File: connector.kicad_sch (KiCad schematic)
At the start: 1 part, among them J4 DIN41612_02x10_AB

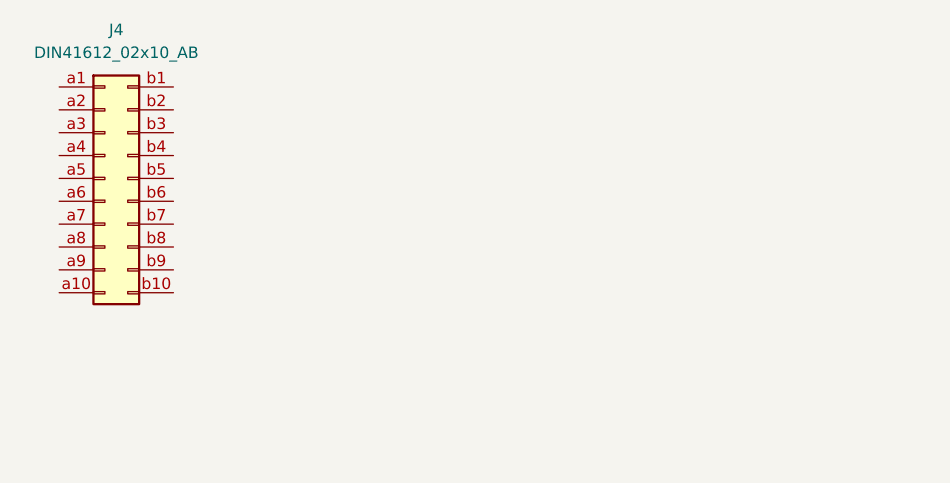
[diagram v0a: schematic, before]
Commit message: updated edge connector
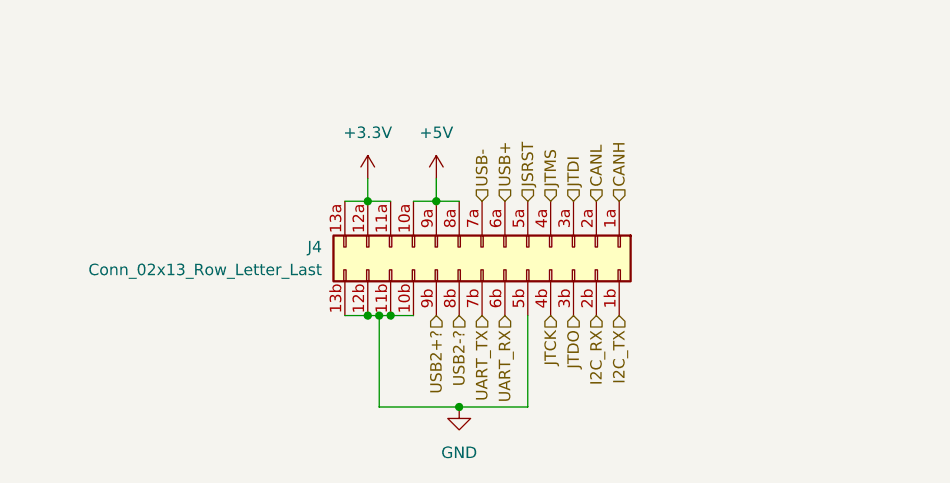
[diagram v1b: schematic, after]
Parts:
- removed J4: DIN41612_02x10_AB, symbol Connector:DIN41612_02x10_AB
- added J4: Conn_02x13_Row_Letter_Last, Connector_Samtec_HSEC8:Samtec_HSEC8-113-X-X-DV_2x13_P0.8mm_Wing_Edge, symbol Connector_Generic:Conn_02x13_Row_Letter_Last
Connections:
- new net +3.3V: J4.11a (Pin_11a), J4.12a (Pin_12a), J4.13a (Pin_13a)
- new net +5V: J4.10a (Pin_10a), J4.8a (Pin_8a), J4.9a (Pin_9a)
- new net CANH: J4.1a (Pin_1a)
- new net CANL: J4.2a (Pin_2a)
- new net GND: J4.10b (Pin_10b), J4.11b (Pin_11b), J4.12b (Pin_12b), J4.13b (Pin_13b), J4.5b (Pin_5b)
- new net I2C_RX: J4.2b (Pin_2b)
- new net I2C_TX: J4.1b (Pin_1b)
- new net JSRST: J4.5a (Pin_5a)
- new net JTCK: J4.4b (Pin_4b)
- new net JTDI: J4.3a (Pin_3a)
- new net JTDO: J4.3b (Pin_3b)
- new net JTMS: J4.4a (Pin_4a)
- new net UART_RX: J4.6b (Pin_6b)
- new net UART_TX: J4.7b (Pin_7b)
- new net USB+: J4.6a (Pin_6a)
- new net USB-: J4.7a (Pin_7a)
- new net USB2+?: J4.9b (Pin_9b)
- new net USB2-?: J4.8b (Pin_8b)

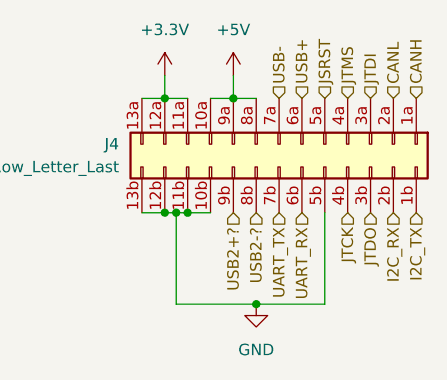
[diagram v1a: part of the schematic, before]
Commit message: renamed i2c
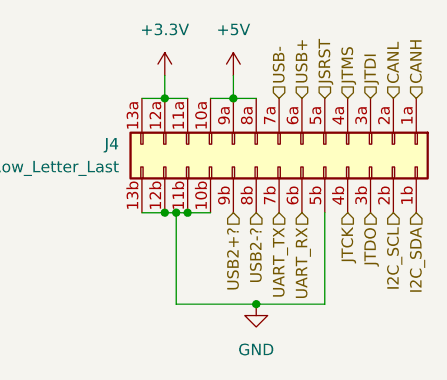
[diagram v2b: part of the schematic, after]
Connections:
- net I2C_RX renamed I2C_SCL
- net I2C_TX renamed I2C_SDA
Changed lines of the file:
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@@
 		)
 	)
-	(hierarchical_label "I2C_RX"
+	(hierarchical_label "I2C_SCL"
 		(shape input)
 		(at 86.36 53.34 270)
@@
 		)
 	)
-	(hierarchical_label "I2C_TX"
+	(hierarchical_label "I2C_SDA"
 		(shape input)
 		(at 88.9 53.34 270)

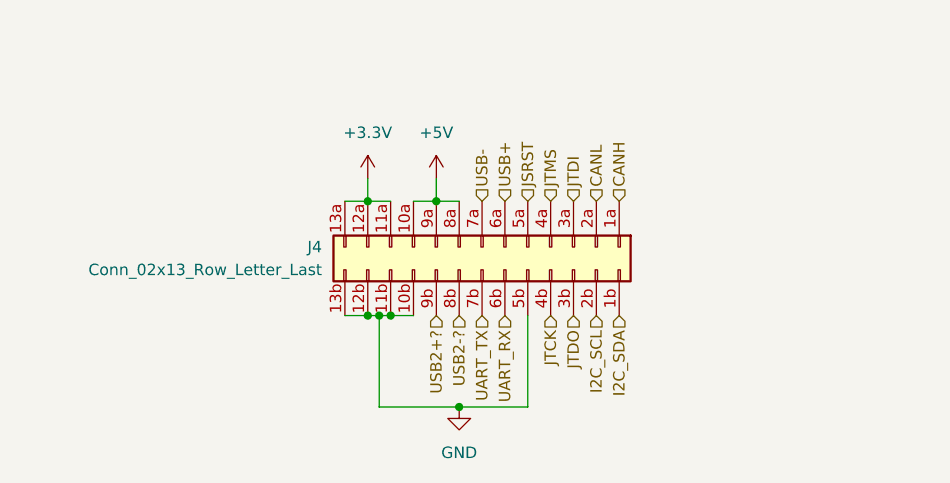
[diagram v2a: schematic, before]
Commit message: started pcb layout, host and usbhub done
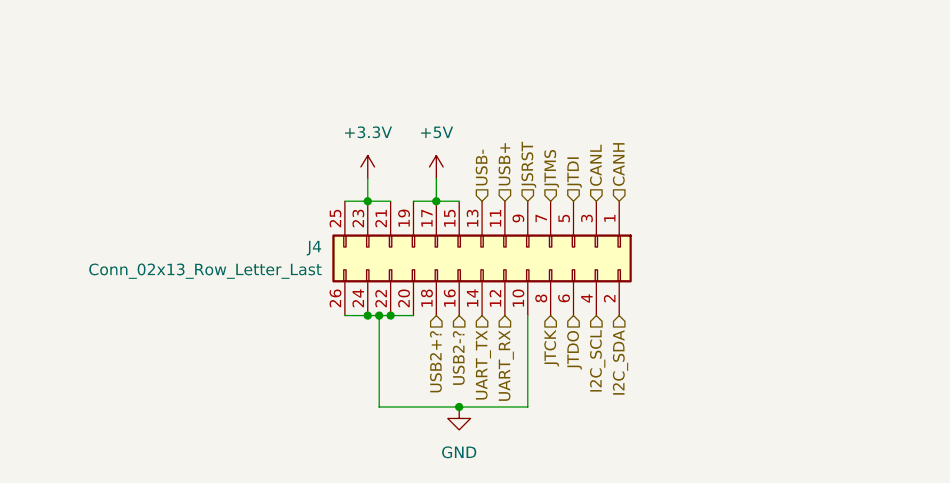
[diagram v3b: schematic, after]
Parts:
- J4: symbol Connector_Generic:Conn_02x13_Row_Letter_Last -> Connector_Generic:Conn_02x13_Odd_Even
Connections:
- net +3.3V: now also J4.21 (Pin_21), J4.23 (Pin_23), J4.25 (Pin_25); no longer J4.11a (Pin_11a), J4.12a (Pin_12a), J4.13a (Pin_13a)
- net +5V: now also J4.15 (Pin_15), J4.17 (Pin_17), J4.19 (Pin_19); no longer J4.10a (Pin_10a), J4.8a (Pin_8a), J4.9a (Pin_9a)
- net CANH: now also J4.1 (Pin_1); no longer J4.1a (Pin_1a)
- net CANL: now also J4.3 (Pin_3); no longer J4.2a (Pin_2a)
- net GND: now also J4.10 (Pin_10), J4.20 (Pin_20), J4.22 (Pin_22), J4.24 (Pin_24), J4.26 (Pin_26); no longer J4.10b (Pin_10b), J4.11b (Pin_11b), J4.12b (Pin_12b), J4.13b (Pin_13b), J4.5b (Pin_5b)
- net I2C_SCL: now also J4.4 (Pin_4); no longer J4.2b (Pin_2b)
- net I2C_SDA: now also J4.2 (Pin_2); no longer J4.1b (Pin_1b)
- net JSRST: now also J4.9 (Pin_9); no longer J4.5a (Pin_5a)
- net JTCK: now also J4.8 (Pin_8); no longer J4.4b (Pin_4b)
- net JTDI: now also J4.5 (Pin_5); no longer J4.3a (Pin_3a)
- net JTDO: now also J4.6 (Pin_6); no longer J4.3b (Pin_3b)
- net JTMS: now also J4.7 (Pin_7); no longer J4.4a (Pin_4a)
- net UART_RX: now also J4.12 (Pin_12); no longer J4.6b (Pin_6b)
- net UART_TX: now also J4.14 (Pin_14); no longer J4.7b (Pin_7b)
- net USB+: now also J4.11 (Pin_11); no longer J4.6a (Pin_6a)
- net USB-: now also J4.13 (Pin_13); no longer J4.7a (Pin_7a)
- net USB2+?: now also J4.18 (Pin_18); no longer J4.9b (Pin_9b)
- net USB2-?: now also J4.16 (Pin_16); no longer J4.8b (Pin_8b)

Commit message: pcb routed!!!!!!!
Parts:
- removed J4: Conn_02x13_Row_Letter_Last, Connector_Samtec_HSEC8:Samtec_HSEC8-113-X-X-DV_2x13_P0.8mm_Wing_Edge, symbol Connector_Generic:Conn_02x13_Odd_Even
- added J3: Conn_02x13_Row_Letter_Last, Connector_Samtec_HSEC8:Samtec_HSEC8-113-X-X-DV_2x13_P0.8mm_Edge, symbol Connector_Generic:Conn_02x13_Odd_Even
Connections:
- net +3.3V: now also J3.1 (Pin_1), J3.3 (Pin_3), J3.5 (Pin_5)
- net +5V: now also J3.11 (Pin_11), J3.7 (Pin_7), J3.9 (Pin_9)
- net CANH: now also J3.25 (Pin_25)
- net CANL: now also J3.23 (Pin_23)
- net GND: now also J3.14 (Pin_14), J3.2 (Pin_2), J3.4 (Pin_4), J3.6 (Pin_6), J3.8 (Pin_8)
- net I2C_SCL: now also J3.24 (Pin_24)
- net I2C_SDA: now also J3.26 (Pin_26)
- net JSRST: now also J3.21 (Pin_21)
- net JTCK: now also J3.20 (Pin_20)
- net JTDI: now also J3.17 (Pin_17)
- net JTDO: now also J3.22 (Pin_22)
- net JTMS: now also J3.19 (Pin_19)
- net UART_RX: now also J3.18 (Pin_18)
- net UART_TX: now also J3.16 (Pin_16)
- net USB+: now also J3.15 (Pin_15)
- net USB-: now also J3.13 (Pin_13)
- net USB2+?: now also J3.10 (Pin_10)
- net USB2-?: now also J3.12 (Pin_12)
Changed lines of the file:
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@@
+	)
+	(junction
+		(at 71.12 63.5)
+		(diameter 0)
+		(color 0 0 0 0)
 	)
 	(junction
@@
 	)
 	(junction
-		(at 71.12 63.5)
-		(diameter 0)
-		(color 0 0 0 0)
-	)
-	(junction
 		(at 60.96 40.64)
 		(diameter 0)
@@
 	(wire
 		(pts
+			(xy 62.23 53.34) (xy 63.5 53.34)
+		)
+		(stroke
+			(width 0)
+			(type default)
+		)
+	)
+	(wire
+		(pts
+			(xy 60.96 40.64) (xy 63.5 40.64)
+		)
+		(stroke
+			(width 0)
+			(type default)
+		)
+	)
+	(wire
+		(pts
+			(xy 62.23 53.34) (xy 62.23 63.5)
+		)
+		(stroke
+			(width 0)
+			(type default)
+		)
+	)
+	(wire
+		(pts
+			(xy 71.12 63.5) (xy 73.66 63.5)
+		)
+		(stroke
+			(width 0)
+			(type default)
+		)
+	)
+	(wire
+		(pts
+			(xy 60.96 53.34) (xy 62.23 53.34)
+		)
+		(stroke
+			(width 0)
+			(type default)
+		)
+	)
+	(wire
+		(pts
+			(xy 60.96 38.1) (xy 60.96 40.64)
+		)
+		(stroke
+			(width 0)
+			(type default)
+		)
+	)
+	(wire
+		(pts
 			(xy 58.42 53.34) (xy 60.96 53.34)
 		)
@@
 	(wire
 		(pts
-			(xy 62.23 53.34) (xy 63.5 53.34)
-		)
-		(stroke
-			(width 0)
-			(type default)
-		)
-	)
-	(wire
-		(pts
-			(xy 60.96 40.64) (xy 63.5 40.64)
-		)
-		(stroke
-			(width 0)
-			(type default)
-		)
-	)
-	(wire
-		(pts
-			(xy 62.23 53.34) (xy 62.23 63.5)
-		)
-		(stroke
-			(width 0)
-			(type default)
-		)
-	)
-	(wire
-		(pts
-			(xy 71.12 63.5) (xy 78.74 63.5)
-		)
-		(stroke
-			(width 0)
-			(type default)
-		)
-	)
-	(wire
-		(pts
-			(xy 60.96 38.1) (xy 60.96 40.64)
-		)
-		(stroke
-			(width 0)
-			(type default)
-		)
-	)
-	(wire
-		(pts
-			(xy 60.96 53.34) (xy 62.23 53.34)
-		)
-		(stroke
-			(width 0)
-			(type default)
-		)
-	)
-	(wire
-		(pts
-			(xy 78.74 63.5) (xy 78.74 53.34)
+			(xy 73.66 53.34) (xy 73.66 63.5)
 		)
 		(stroke
@@
 		)
 	)
+	(hierarchical_label "JTCK"
+		(shape input)
+		(at 81.28 53.34 270)
+		(fields_autoplaced yes)
+		(effects
+			(font
+				(size 1.27 1.27)
+			)
+			(justify right)
+		)
+	)
+	(hierarchical_label "USB+"
+		(shape input)
+		(at 76.2 40.64 90)
+		(fields_autoplaced yes)
+		(effects
+			(font
+				(size 1.27 1.27)
+			)
+			(justify left)
+		)
+	)
+	(hierarchical_label "UART_TX"
+		(shape input)
+		(at 76.2 53.34 270)
+		(fields_autoplaced yes)
+		(effects
+			(font
+				(size 1.27 1.27)
+			)
+			(justify right)
+		)
+	)
+	(hierarchical_label "USB-"
+		(shape input)
+		(at 73.66 40.64 90)
+		(fields_autoplaced yes)
+		(effects
+			(font
+				(size 1.27 1.27)
+			)
+			(justify left)
+		)
+	)
+	(hierarchical_label "CANH"
+		(shape input)
+		(at 88.9 40.64 90)
+		(fields_autoplaced yes)
+		(effects
+			(font
+				(size 1.27 1.27)
+			)
+			(justify left)
+		)
+	)
+	(hierarchical_label "I2C_SCL"
+		(shape input)
+		(at 86.36 53.34 270)
+		(fields_autoplaced yes)
+		(effects
+			(font
+				(size 1.27 1.27)
+			)
+			(justify right)
+		)
+	)
+	(hierarchical_label "CANL"
+		(shape input)
+		(at 86.36 40.64 90)
+		(fields_autoplaced yes)
+		(effects
+			(font
+				(size 1.27 1.27)
+			)
+			(justify left)
+		)
+	)
+	(hierarchical_label "JTDI"
+		(shape input)
+		(at 78.74 40.64 90)
+		(fields_autoplaced yes)
+		(effects
+			(font
+				(size 1.27 1.27)
+			)
+			(justify left)
+		)
+	)
+	(hierarchical_label "JTMS"
+		(shape input)
+		(at 81.28 40.64 90)
+		(fields_autoplaced yes)
+		(effects
+			(font
+				(size 1.27 1.27)
+			)
+			(justify left)
+		)
+	)
+	(hierarchical_label "I2C_SDA"
+		(shape input)
+		(at 88.9 53.34 270)
+		(fields_autoplaced yes)
+		(effects
+			(font
+				(size 1.27 1.27)
+			)
+			(justify right)
+		)
+	)
 	(hierarchical_label "UART_RX"
 		(shape input)
-		(at 76.2 53.34 270)
-		(fields_autoplaced yes)
-		(effects
-			(font
-				(size 1.27 1.27)
-			)
-			(justify right)
-		)
-	)
-	(hierarchical_label "JTCK"
-		(shape input)
-		(at 81.28 53.34 270)
-		(fields_autoplaced yes)
-		(effects
-			(font
-				(size 1.27 1.27)
-			)
-			(justify right)
-		)
-	)
-	(hierarchical_label "USB+"
-		(shape input)
-		(at 76.2 40.64 90)
+		(at 78.74 53.34 270)
+		(fields_autoplaced yes)
+		(effects
+			(font
+				(size 1.27 1.27)
+			)
+			(justify right)
+		)
+	)
+	(hierarchical_label "JTDO"
+		(shape input)
+		(at 83.82 53.34 270)
+		(fields_autoplaced yes)
+		(effects
+			(font
+				(size 1.27 1.27)
+			)
+			(justify right)
+		)
+	)
+	(hierarchical_label "USB2-?"
+		(shape input)
+		(at 71.12 53.34 270)
+		(fields_autoplaced yes)
+		(effects
+			(font
+				(size 1.27 1.27)
+			)
+			(justify right)
+		)
+	)
+	(hierarchical_label "JSRST"
+		(shape input)
+		(at 83.82 40.64 90)
 		(fields_autoplaced yes)
 		(effects
@@
 			)
 			(justify left)
-		)
-	)
-	(hierarchical_label "USB-"
-		(shape input)
-		(at 73.66 40.64 90)
-		(fields_autoplaced yes)
-		(effects
-			(font
-				(size 1.27 1.27)
-			)
-			(justify left)
-		)
-	)
-	(hierarchical_label "CANH"
-		(shape input)
-		(at 88.9 40.64 90)
-		(fields_autoplaced yes)
-		(effects
-			(font
-				(size 1.27 1.27)
-			)
-			(justify left)
-		)
-	)
-	(hierarchical_label "I2C_SCL"
-		(shape input)
-		(at 86.36 53.34 270)
-		(fields_autoplaced yes)
-		(effects
-			(font
-				(size 1.27 1.27)
-			)
-			(justify right)
-		)
-	)
-	(hierarchical_label "CANL"
-		(shape input)
-		(at 86.36 40.64 90)
-		(fields_autoplaced yes)
-		(effects
-			(font
-				(size 1.27 1.27)
-			)
-			(justify left)
-		)
-	)
-	(hierarchical_label "JTMS"
-		(shape input)
-		(at 81.28 40.64 90)
-		(fields_autoplaced yes)
-		(effects
-			(font
-				(size 1.27 1.27)
-			)
-			(justify left)
-		)
-	)
-	(hierarchical_label "UART_TX"
-		(shape input)
-		(at 73.66 53.34 270)
-		(fields_autoplaced yes)
-		(effects
-			(font
-				(size 1.27 1.27)
-			)
-			(justify right)
-		)
-	)
-	(hierarchical_label "JTDI"
-		(shape input)
-		(at 83.82 40.64 90)
-		(fields_autoplaced yes)
-		(effects
-			(font
-				(size 1.27 1.27)
-			)
-			(justify left)
-		)
-	)
-	(hierarchical_label "JSRST"
-		(shape input)
-		(at 78.74 40.64 90)
-		(fields_autoplaced yes)
-		(effects
-			(font
-				(size 1.27 1.27)
-			)
-			(justify left)
-		)
-	)
-	(hierarchical_label "I2C_SDA"
-		(shape input)
-		(at 88.9 53.34 270)
-		(fields_autoplaced yes)
-		(effects
-			(font
-				(size 1.27 1.27)
-			)
-			(justify right)
-		)
-	)
-	(hierarchical_label "JTDO"
-		(shape input)
-		(at 83.82 53.34 270)
-		(fields_autoplaced yes)
-		(effects
-			(font
-				(size 1.27 1.27)
-			)
-			(justify right)
-		)
-	)
-	(hierarchical_label "USB2-?"
-		(shape input)
-		(at 71.12 53.34 270)
-		(fields_autoplaced yes)
-		(effects
-			(font
-				(size 1.27 1.27)
-			)
-			(justify right)
 		)
 	)
@@
 	(symbol
 		(lib_id "Connector_Generic:Conn_02x13_Odd_Even")
-		(at 73.66 45.72 270)
+		(at 73.66 45.72 90)
+		(mirror x)
 		(unit 1)
 		(exclude_from_sim no)
@@
 		(on_board yes)
 		(dnp no)
-		(property "Reference" "J4"
-			(at 55.88 45.7199 90)
+		(property "Reference" "J3"
+			(at 91.44 45.7199 90)
 			(effects
 				(font
@@
 		)
 		(property "Value" "Conn_02x13_Row_Letter_Last"
-			(at 55.88 48.2599 90)
+			(at 91.44 48.2599 90)
 			(effects
 				(font
@@
 			)
 		)
-		(property "Footprint" "Connector_Samtec_HSEC8:Samtec_HSEC8-113-X-X-DV_2x13_P0.8mm_Wing_Edge"
+		(property "Footprint" "Connector_Samtec_HSEC8:Samtec_HSEC8-113-X-X-DV_2x13_P0.8mm_Edge"
 			(at 73.66 45.72 0)
 			(effects
@@
 		)
 		(instances
-			(project ""
+			(project "debug_board"
 				(path "/9ba02813-5189-4482-9c9e-35a29bc7aded/c341ef78-2e89-4134-9acd-82690de25dd5"
-					(reference "J4")
+					(reference "J3")
 					(unit 1)
 				)
